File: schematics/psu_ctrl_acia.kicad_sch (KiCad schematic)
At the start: 3 parts

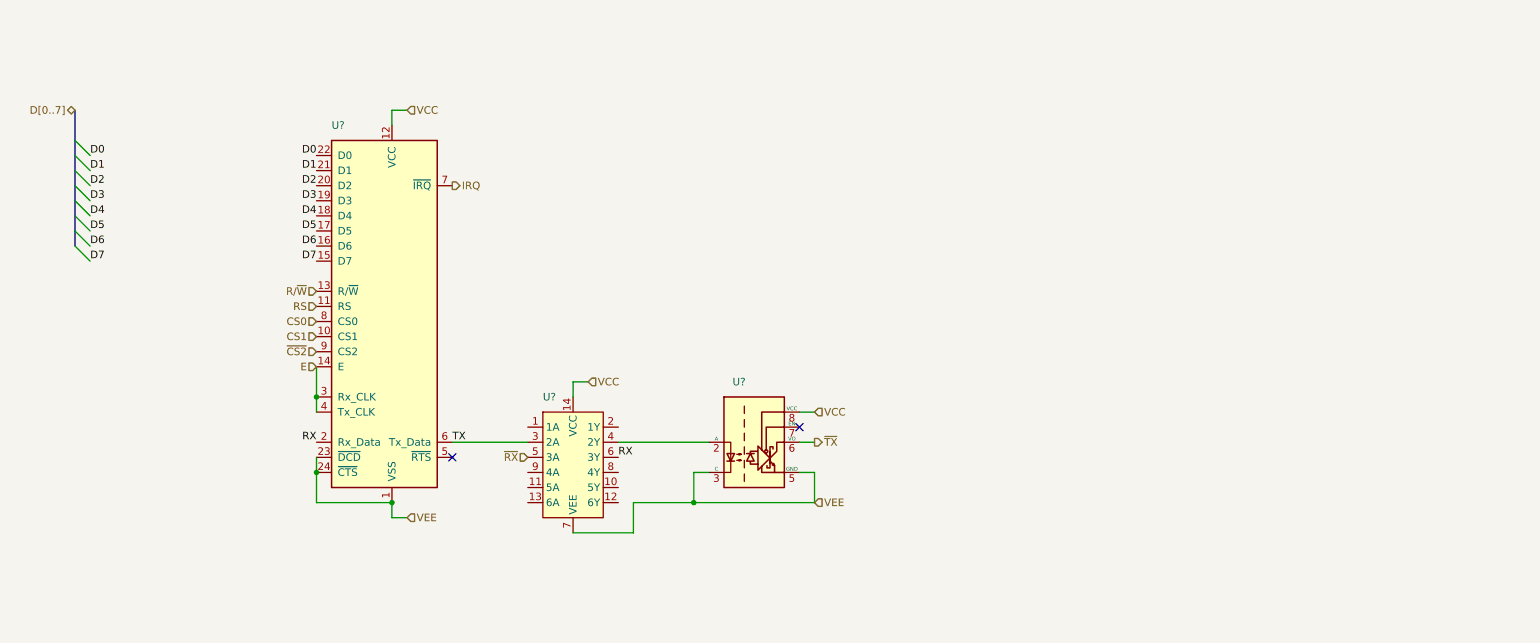
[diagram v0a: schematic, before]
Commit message: Moved more components into hierachical sheets, misc cleanup
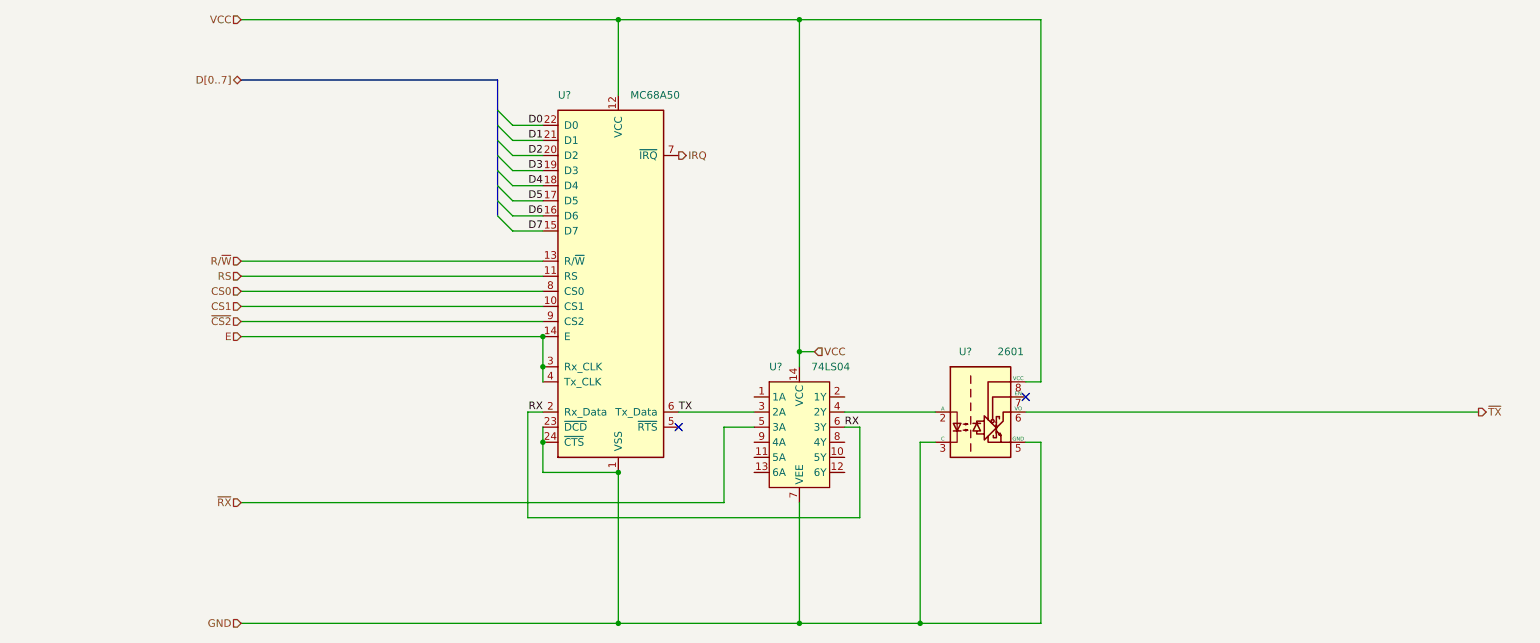
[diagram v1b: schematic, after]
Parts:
- U?: value ~ -> 74LS04
- U?: value ~ -> MC68A50
- U?: value ~ -> 2601
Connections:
- net VEE renamed GND
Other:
- moved on the sheet: U?

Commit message: cleanup, fixes, started on power supplies
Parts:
- removed U?: 2601, symbol Isolator:HCPL-2601
- added C15, C7: 0u1, symbol Device:C_Small
- added R1: 330, symbol Device:R_Small
- IC13: renamed from U?; footprint (none) -> Package_DIP:DIP-40_W15.24mm
- gave numbers to parts that had none: 1
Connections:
- net GND: now also C15.2, C7.2, R1.2
- net VCC: now also C15.1, C7.1
- net ~{RX}: now also R1.1
- net ~{TX}: now also IC7.4 (2Y)
- no-connect marks 2 -> 9

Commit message: More power supply work
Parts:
- IC7: value 74LS04 -> 74LD04
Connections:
- net RS renamed RD
